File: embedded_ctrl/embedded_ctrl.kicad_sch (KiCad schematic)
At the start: 50 parts, among them J1 Conn_02x13_Odd_Even, J2 RJ11, J3 Conn_01x15_Socket, J4 Conn_01x15_Socket, J5 RJ11, J6 Screw_Terminal_01x02, J7 USB_B, Q1 SS8050, Q2 SS8050, U1 ESP32-WROOM-32, U2 CP2102N-A02-GQFN28, U3 R-78E3.3-1.0

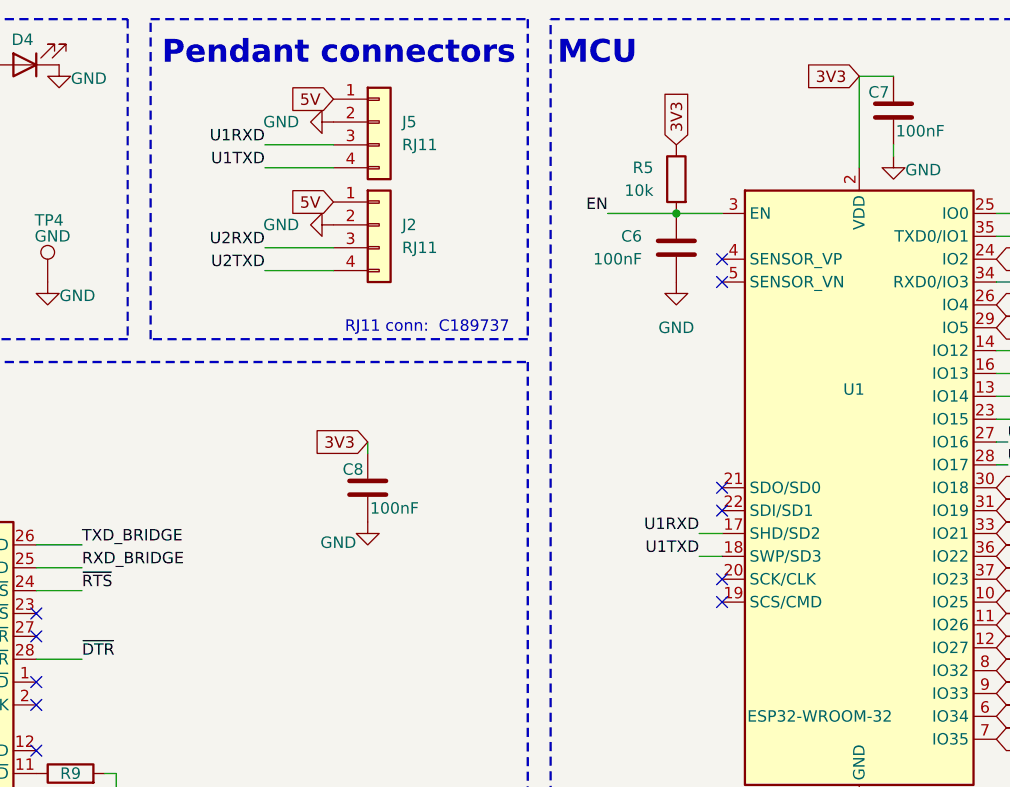
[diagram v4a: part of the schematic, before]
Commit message: Don't use UART1 - its pins are already in use for the SPI flash
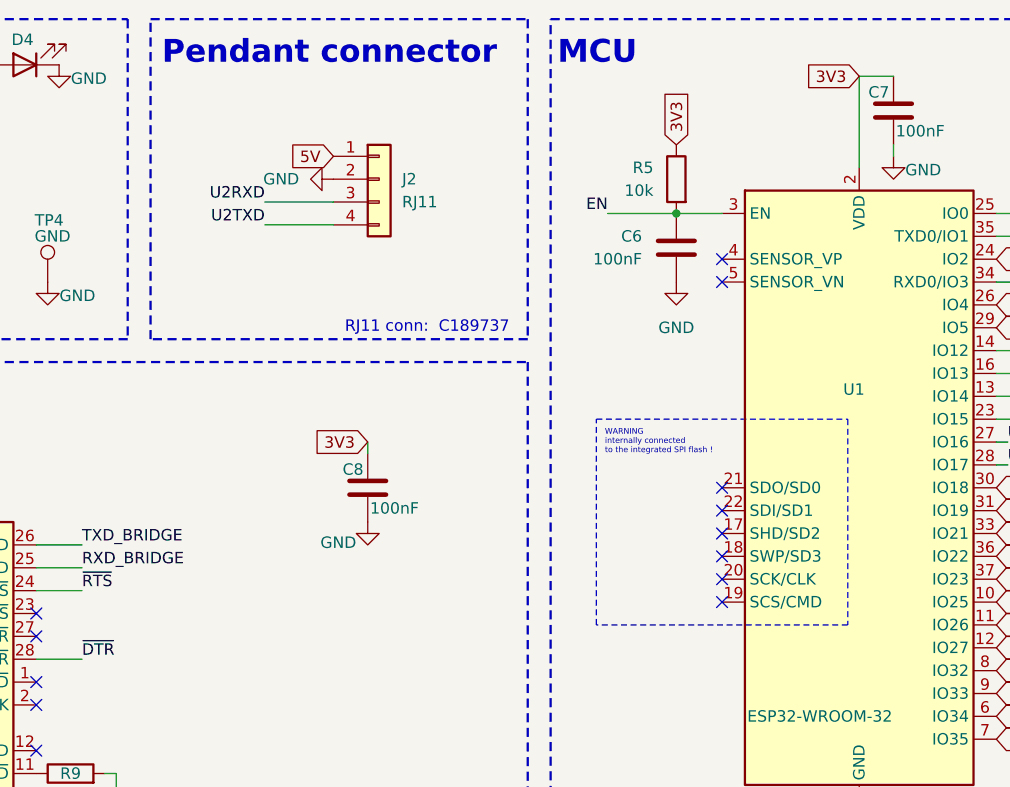
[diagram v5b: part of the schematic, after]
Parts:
- removed J5: RJ11, Library:RJ11_C189737, symbol Connector_Generic:Conn_01x04
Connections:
- net U1RXD: no longer names the net of U1.17 (SHD/SD2)
- net U1TXD: no longer names the net of U1.18 (SWP/SD3)
- no-connect marks 23 -> 25
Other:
- note added: "Pendant connector"
- note removed: "Pendant connectors"
- moved on the sheet: J2

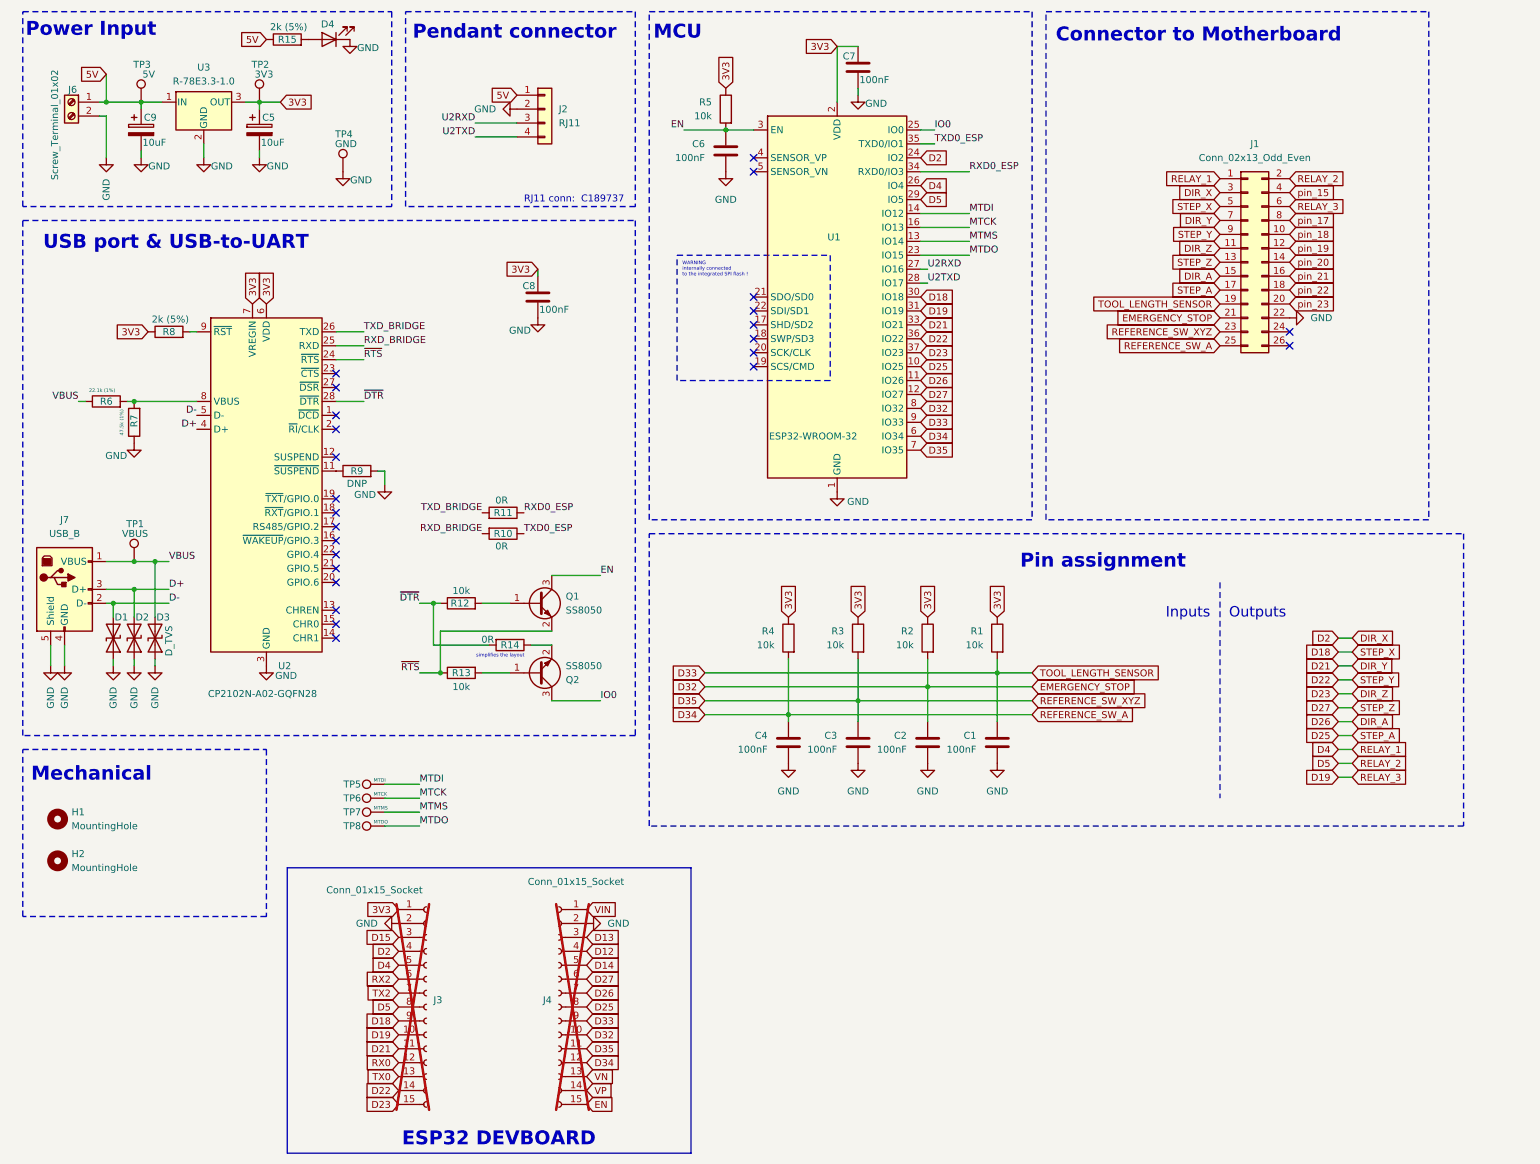
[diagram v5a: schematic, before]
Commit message: Expose D36 and D39. Add buttons for EN and IO0,bodge wire passthrus, and version text
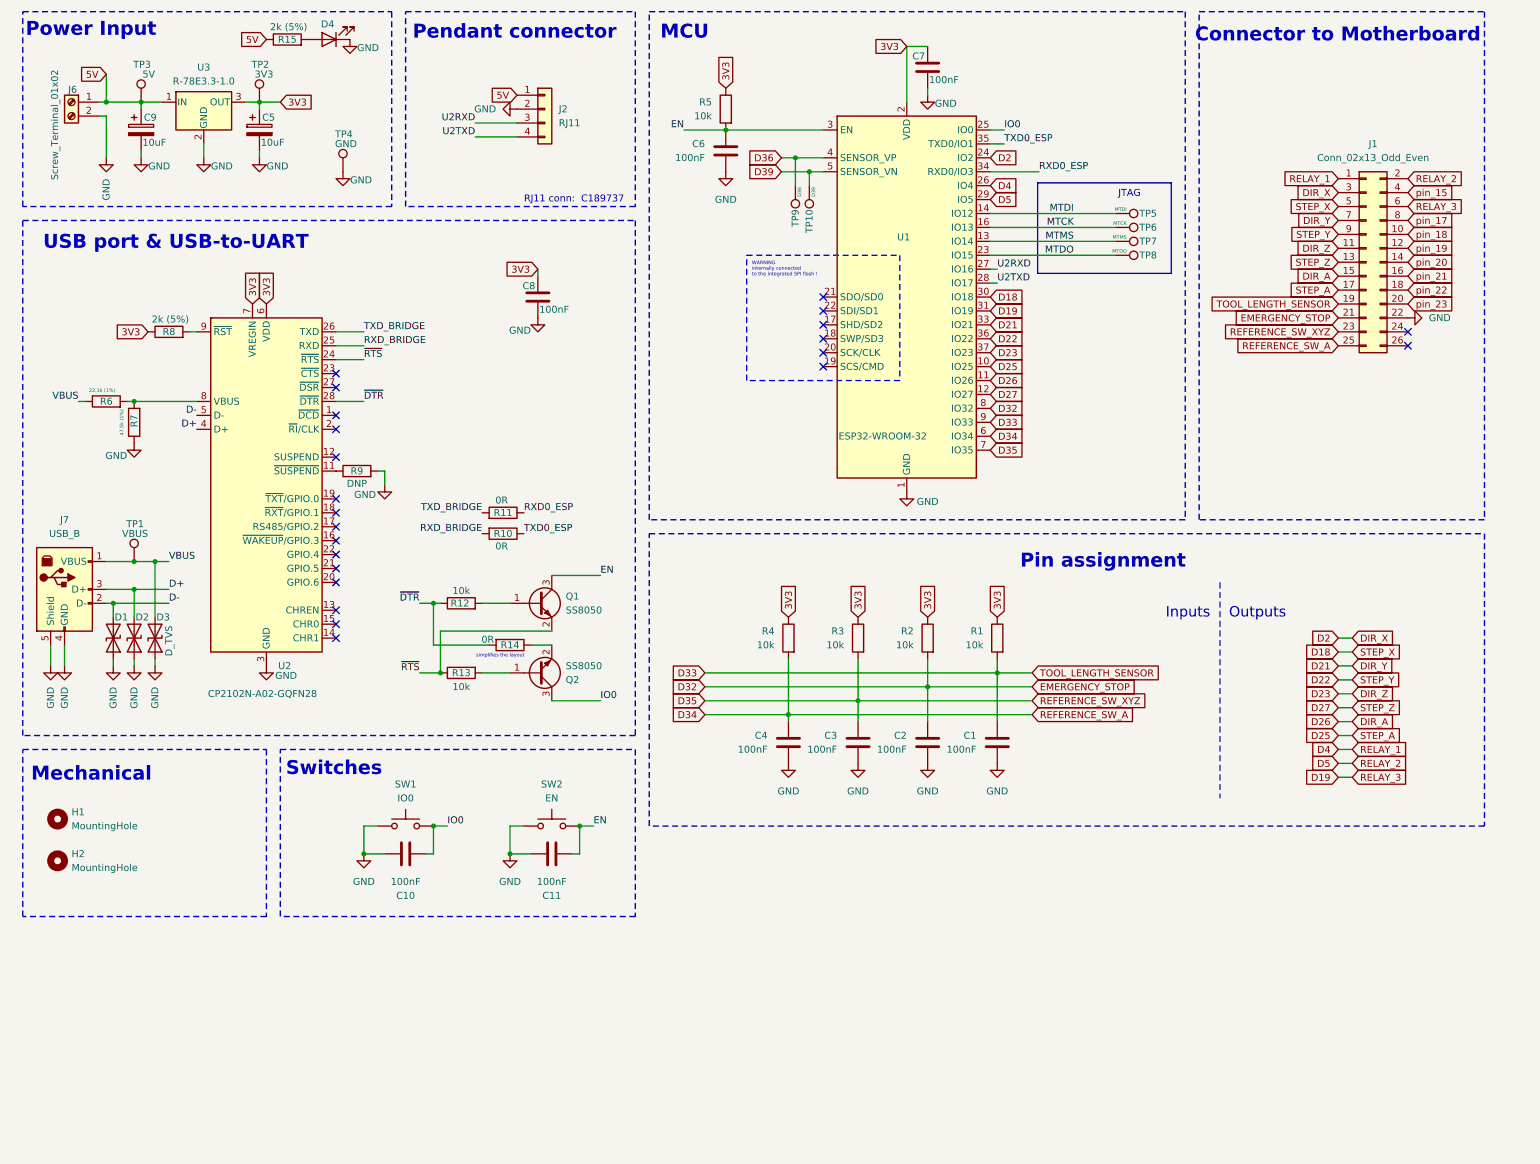
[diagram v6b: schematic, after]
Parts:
- removed J3, J4: Conn_01x15_Socket, symbol Connector:Conn_01x15_Socket
- added C10, C11: 100nF, Capacitor_SMD:C_0603_1608Metric, symbol Device:C
- added SW1: IO0, Button_Switch_SMD:SW_Push_1P1T_NO_Vertical_Wuerth_434133025816, symbol Switch:SW_Push
- added SW2: EN, Button_Switch_SMD:SW_Push_1P1T_NO_Vertical_Wuerth_434133025816, symbol Switch:SW_Push
- added TP10: D39, TestPoint:TestPoint_Pad_D1.0mm, symbol Connector:TestPoint
- added TP9: D36, TestPoint:TestPoint_Pad_D1.0mm, symbol Connector:TestPoint
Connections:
- net EN: now also C11.1, SW2.2
- net GND: now also C10.2, C11.2, SW1.1, SW2.1
- net IO0: now also C10.1, SW1.2
- net D36: now reaches U1.4 (SENSOR_VP)
- net D36: now also TP9.1
- net D39: now reaches U1.5 (SENSOR_VN)
- net D39: now also TP10.1
- no-connect marks 25 -> 23
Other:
- note added: "JTAG"
- note added: "Switches"
- note removed: "ESP32 DEVBOARD"
- moved on the sheet: C7, J1, TP5, TP6, TP7, TP8, U1

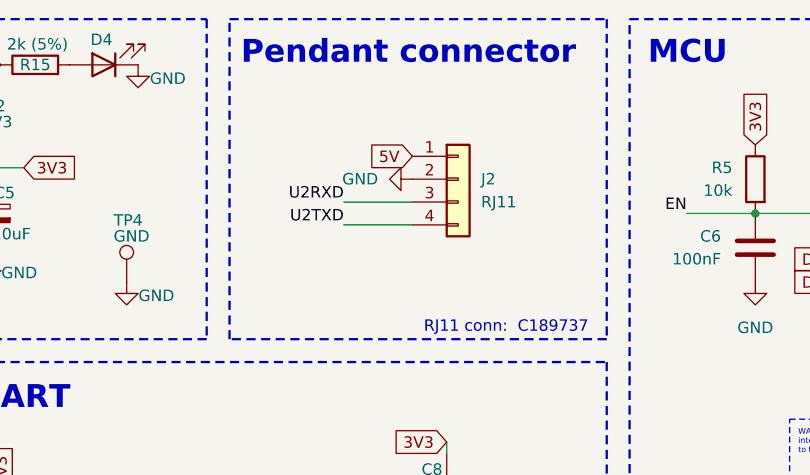
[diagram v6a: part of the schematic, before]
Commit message: add tvs diodes to uart connector
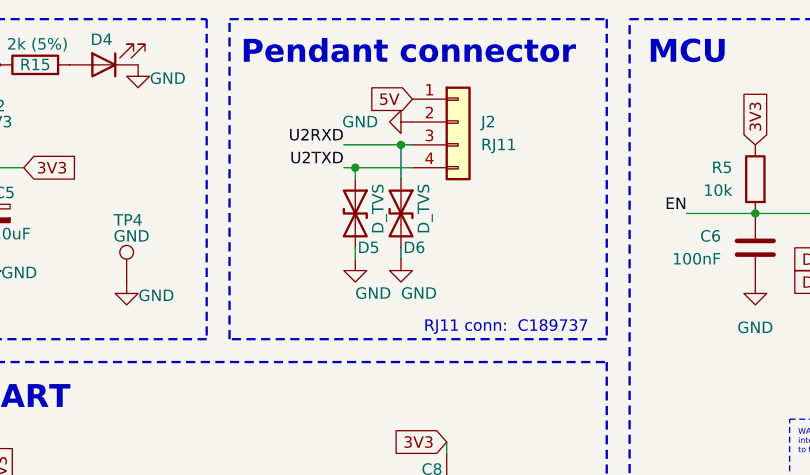
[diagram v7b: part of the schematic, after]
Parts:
- added D5, D6: D_TVS, Diode_SMD:D_0603_1608Metric, symbol Device:D_TVS
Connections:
- net GND: now also D5.2 (A2), D6.2 (A2)
- net U2RXD: now also D6.1 (A1)
- net U2TXD: now also D5.1 (A1)
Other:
- moved on the sheet: J2
